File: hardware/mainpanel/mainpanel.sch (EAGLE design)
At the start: 0 parts

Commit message: Add Nucleo board
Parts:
- added B1: (no value), Frcy:NUCLEO-32

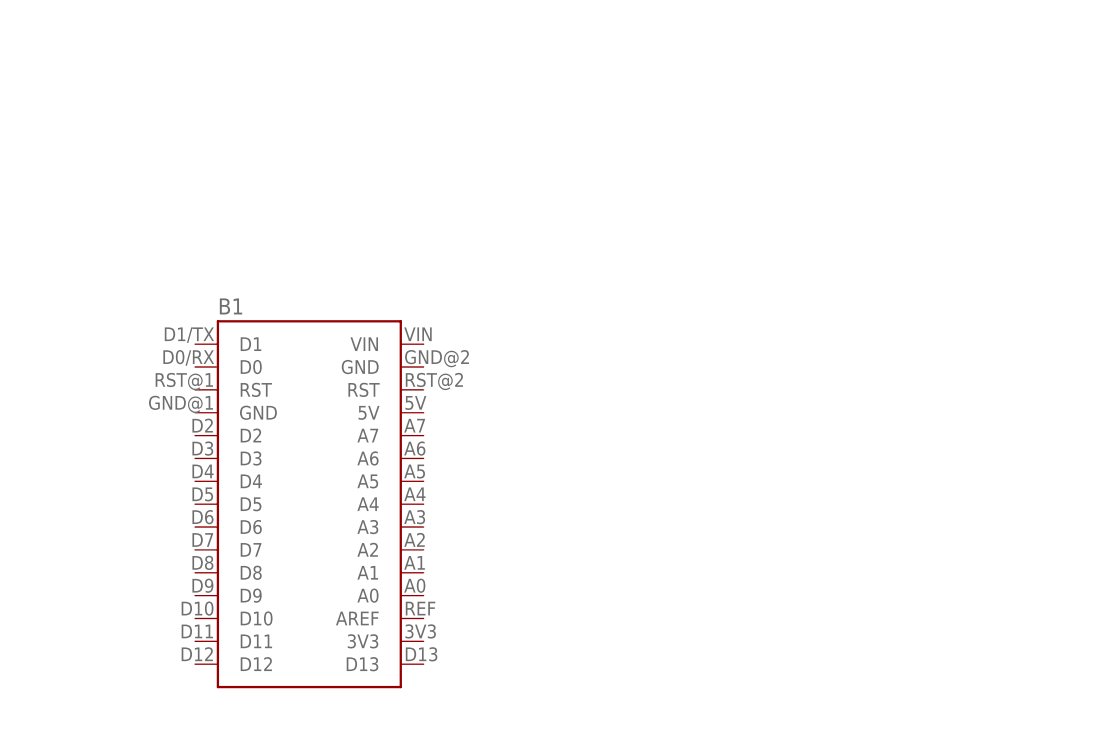
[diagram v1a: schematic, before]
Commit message: Add BNO055 and connections
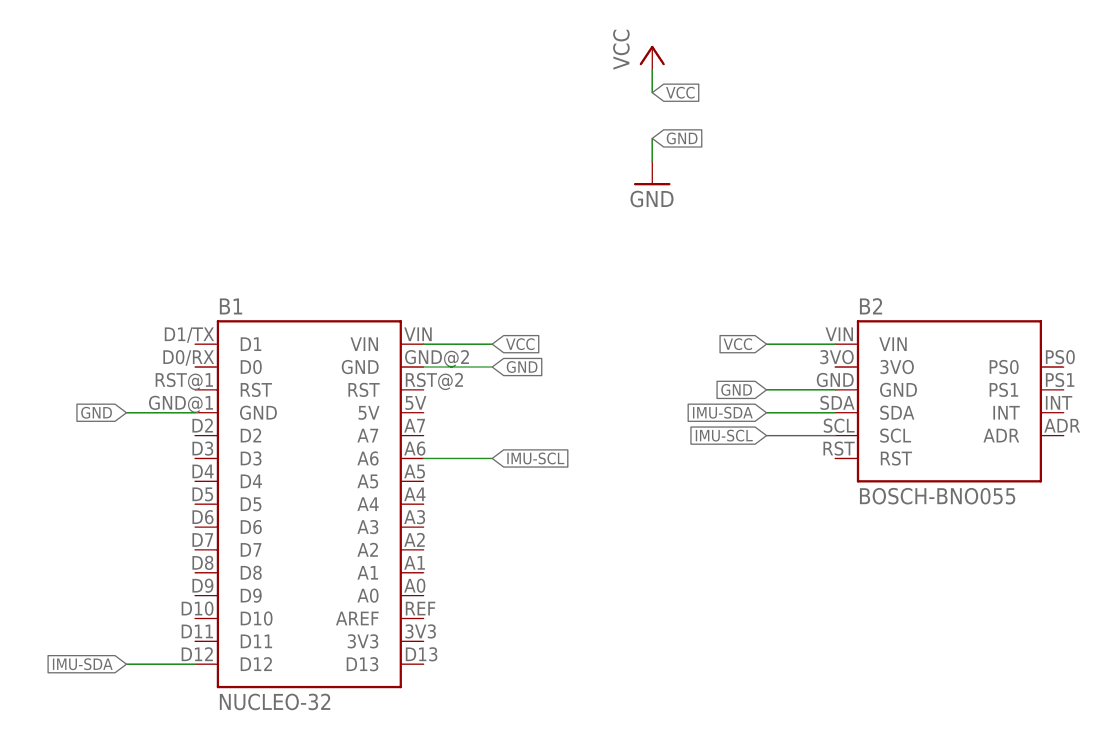
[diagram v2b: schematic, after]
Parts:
- added B2: BOSCH-BNO055, Frcy:BOSCH-BNO055
- B1: value (none) -> NUCLEO-32
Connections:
- new net GND: B1.GND@1, B1.GND@2, B2.GND
- new net IMU-SCL: B1.A6, B2.SCL
- new net IMU-SDA: B1.D12, B2.SDA
- new net VCC: B1.VIN, B2.VIN
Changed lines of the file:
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@@
 <part name="FRAME1" library="frames" library_urn="urn:adsk.eagle:library:229" deviceset="DINA4_L" device=""/>
 <part name="B1" library="Frcy" deviceset="NUCLEO-32" device=""/>
+<part name="B2" library="Frcy" deviceset="BOSCH-BNO055" device=""/>
+<part name="P+1" library="supply1" library_urn="urn:adsk.eagle:library:371" deviceset="VCC" device=""/>
+<part name="GND1" library="supply1" library_urn="urn:adsk.eagle:library:371" deviceset="GND" device=""/>
 </parts>
 <sheets>
@@
 <instance part="FRAME1" gate="G$2" x="162.56" y="0"/>
 <instance part="B1" gate="G$1" x="119.38" y="106.68"/>
+<instance part="B2" gate="G$1" x="190.5" y="119.38"/>
+<instance part="P+1" gate="VCC" x="157.48" y="157.48"/>
+<instance part="GND1" gate="1" x="157.48" y="142.24"/>
 </instances>
 <busses>
 </busses>
 <nets>
+<net name="VCC" class="0">
+<segment>
+<pinref part="P+1" gate="VCC" pin="VCC"/>
+<wire x1="157.48" y1="154.94" x2="157.48" y2="152.4" width="0.1524" layer="91"/>
+<label x="157.48" y="152.4" size="1.27" layer="95" xref="yes"/>
+</segment>
+<segment>
+<pinref part="B1" gate="G$1" pin="VIN"/>
+<wire x1="132.08" y1="124.46" x2="139.7" y2="124.46" width="0.1524" layer="91"/>
+<label x="139.7" y="124.46" size="1.27" layer="95" xref="yes"/>
+</segment>
+<segment>
+<pinref part="B2" gate="G$1" pin="VIN"/>
+<wire x1="177.8" y1="124.46" x2="170.18" y2="124.46" width="0.1524" layer="91"/>
+<label x="170.18" y="124.46" size="1.27" layer="95" rot="R180" xref="yes"/>
+</segment>
+</net>
+<net name="GND" class="0">
+<segment>
+<pinref part="GND1" gate="1" pin="GND"/>
+<wire x1="157.48" y1="144.78" x2="157.48" y2="147.32" width="0.1524" layer="91"/>
+<label x="157.48" y="147.32" size="1.27" layer="95" xref="yes"/>
+</segment>
+<segment>
+<pinref part="B1" gate="G$1" pin="GND@2"/>
+<wire x1="132.08" y1="121.92" x2="139.7" y2="121.92" width="0.1524" layer="91"/>
+<label x="139.7" y="121.92" size="1.27" layer="95" xref="yes"/>
+</segment>
+<segment>
+<pinref part="B1" gate="G$1" pin="GND@1"/>
+<wire x1="106.68" y1="116.84" x2="99.06" y2="116.84" width="0.1524" layer="91"/>
+<label x="99.06" y="116.84" size="1.27" layer="95" rot="R180" xref="yes"/>
+</segment>
+<segment>
+<pinref part="B2" gate="G$1" pin="GND"/>
+<wire x1="177.8" y1="119.38" x2="170.18" y2="119.38" width="0.1524" layer="91"/>
+<label x="170.18" y="119.38" size="1.27" layer="95" rot="R180" xref="yes"/>
+</segment>
+</net>
+<net name="IMU-SDA" class="0">
+<segment>
+<pinref part="B2" gate="G$1" pin="SDA"/>
+<wire x1="177.8" y1="116.84" x2="170.18" y2="116.84" width="0.1524" layer="91"/>
+<label x="170.18" y="116.84" size="1.27" layer="95" rot="R180" xref="yes"/>
+</segment>
+<segment>
+<pinref part="B1" gate="G$1" pin="D12"/>
+<wire x1="106.68" y1="88.9" x2="99.06" y2="88.9" width="0.1524" layer="91"/>
+<label x="99.06" y="88.9" size="1.27" layer="95" rot="R180" xref="yes"/>
+</segment>
+</net>
+<net name="IMU-SCL" class="0">
+<segment>
+<pinref part="B2" gate="G$1" pin="SCL"/>
+<wire x1="177.8" y1="114.3" x2="170.18" y2="114.3" width="0.1524" layer="91"/>
+<label x="170.18" y="114.3" size="1.27" layer="95" rot="R180" xref="yes"/>
+</segment>
+<segment>
+<pinref part="B1" gate="G$1" pin="A6"/>
+<wire x1="132.08" y1="111.76" x2="139.7" y2="111.76" width="0.1524" layer="91"/>
+<label x="139.7" y="111.76" size="1.27" layer="95" xref="yes"/>
+</segment>
+</net>
 </nets>
 </sheet>

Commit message: Add components to sch
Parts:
- added B3: (no value), Frcy:UPUTRONICS-UBLOX-PICO
- added B4: (no value), Frcy:SPARKFUN-OPENLOG
- B1: value NUCLEO-32 -> (none)
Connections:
- new net CDH-RX: B1.D0
- new net CDH-TX: B1.D1
- new net GPS-SCL: B1.D5, B3.SCL
- new net GPS-SDA: B1.D4, B3.SDA
- new net LOG-UART: B1.A7, B4.RXI
- new net SPI-CS-ADC: B1.D6
- new net SPI-CS-ENV: B1.D3
- new net SPI-MISO: B1.A5
- new net SPI-MOSI: B1.D2
- new net SPI-SCK: B1.A1
- new net TEMP-OW: B1.D9
- net GND: now also B3.GND, B4.GND
- net VCC: now also B3.VCC, B4.VCC
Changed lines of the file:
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@@
 <part name="P+1" library="supply1" library_urn="urn:adsk.eagle:library:371" deviceset="VCC" device=""/>
 <part name="GND1" library="supply1" library_urn="urn:adsk.eagle:library:371" deviceset="GND" device=""/>
+<part name="B3" library="Frcy" deviceset="UPUTRONICS-UBLOX-PICO" device=""/>
+<part name="B4" library="Frcy" deviceset="SPARKFUN-OPENLOG" device=""/>
 </parts>
 <sheets>
@@
 <instance part="P+1" gate="VCC" x="157.48" y="157.48"/>
 <instance part="GND1" gate="1" x="157.48" y="142.24"/>
+<instance part="B3" gate="G$1" x="182.88" y="91.44"/>
+<instance part="B4" gate="G$1" x="185.42" y="66.04"/>
 </instances>
 <busses>
@@
 <wire x1="177.8" y1="124.46" x2="170.18" y2="124.46" width="0.1524" layer="91"/>
 <label x="170.18" y="124.46" size="1.27" layer="95" rot="R180" xref="yes"/>
+</segment>
+<segment>
+<pinref part="B3" gate="G$1" pin="VCC"/>
+<wire x1="177.8" y1="86.36" x2="170.18" y2="86.36" width="0.1524" layer="91"/>
+<label x="170.18" y="86.36" size="1.27" layer="95" rot="R180" xref="yes"/>
+</segment>
+<segment>
+<pinref part="B4" gate="G$1" pin="VCC"/>
+<wire x1="177.8" y1="66.04" x2="170.18" y2="66.04" width="0.1524" layer="91"/>
+<label x="170.18" y="66.04" size="1.27" layer="95" rot="R180" xref="yes"/>
 </segment>
 </net>
@@
 <wire x1="177.8" y1="119.38" x2="170.18" y2="119.38" width="0.1524" layer="91"/>
 <label x="170.18" y="119.38" size="1.27" layer="95" rot="R180" xref="yes"/>
+</segment>
+<segment>
+<pinref part="B3" gate="G$1" pin="GND"/>
+<wire x1="177.8" y1="88.9" x2="170.18" y2="88.9" width="0.1524" layer="91"/>
+<label x="170.18" y="88.9" size="1.27" layer="95" rot="R180" xref="yes"/>
+</segment>
+<segment>
+<pinref part="B4" gate="G$1" pin="GND"/>
+<wire x1="177.8" y1="63.5" x2="170.18" y2="63.5" width="0.1524" layer="91"/>
+<label x="170.18" y="63.5" size="1.27" layer="95" rot="R180" xref="yes"/>
 </segment>
 </net>
@@
 </segment>
 </net>
+<net name="GPS-SDA" class="0">
+<segment>
+<pinref part="B3" gate="G$1" pin="SDA"/>
+<wire x1="177.8" y1="99.06" x2="170.18" y2="99.06" width="0.1524" layer="91"/>
+<label x="170.18" y="99.06" size="1.27" layer="95" rot="R180" xref="yes"/>
+</segment>
+<segment>
+<pinref part="B1" gate="G$1" pin="D4"/>
+<wire x1="106.68" y1="109.22" x2="99.06" y2="109.22" width="0.1524" layer="91"/>
+<label x="99.06" y="109.22" size="1.27" layer="95" rot="R180" xref="yes"/>
+</segment>
+</net>
+<net name="GPS-SCL" class="0">
+<segment>
+<pinref part="B3" gate="G$1" pin="SCL"/>
+<wire x1="177.8" y1="96.52" x2="170.18" y2="96.52" width="0.1524" layer="91"/>
+<label x="170.18" y="96.52" size="1.27" layer="95" rot="R180" xref="yes"/>
+</segment>
+<segment>
+<pinref part="B1" gate="G$1" pin="D5"/>
+<wire x1="106.68" y1="106.68" x2="99.06" y2="106.68" width="0.1524" layer="91"/>
+<label x="99.06" y="106.68" size="1.27" layer="95" rot="R180" xref="yes"/>
+</segment>
+</net>
+<net name="LOG-UART" class="0">
+<segment>
+<pinref part="B4" gate="G$1" pin="RXI"/>
+<wire x1="177.8" y1="71.12" x2="170.18" y2="71.12" width="0.1524" layer="91"/>
+<label x="170.18" y="71.12" size="1.27" layer="95" rot="R180" xref="yes"/>
+</segment>
+<segment>
+<pinref part="B1" gate="G$1" pin="A7"/>
+<wire x1="132.08" y1="114.3" x2="139.7" y2="114.3" width="0.1524" layer="91"/>
+<label x="139.7" y="114.3" size="1.27" layer="95" xref="yes"/>
+</segment>
+</net>
+<net name="CDH-TX" class="0">
+<segment>
+<pinref part="B1" gate="G$1" pin="D1"/>
+<wire x1="106.68" y1="124.46" x2="99.06" y2="124.46" width="0.1524" layer="91"/>
+<label x="99.06" y="124.46" size="1.27" layer="95" rot="R180" xref="yes"/>
+</segment>
+</net>
+<net name="CDH-RX" class="0">
+<segment>
+<pinref part="B1" gate="G$1" pin="D0"/>
+<wire x1="106.68" y1="121.92" x2="99.06" y2="121.92" width="0.1524" layer="91"/>
+<label x="99.06" y="121.92" size="1.27" layer="95" rot="R180" xref="yes"/>
+</segment>
+</net>
+<net name="SPI-MOSI" class="0">
+<segment>
+<pinref part="B1" gate="G$1" pin="D2"/>
+<wire x1="106.68" y1="114.3" x2="99.06" y2="114.3" width="0.1524" layer="91"/>
+<label x="99.06" y="114.3" size="1.27" layer="95" rot="R180" xref="yes"/>
+</segment>
+</net>
+<net name="SPI-CS-ADC" class="0">
+<segment>
+<pinref part="B1" gate="G$1" pin="D6"/>
+<wire x1="106.68" y1="104.14" x2="99.06" y2="104.14" width="0.1524" layer="91"/>
+<label x="99.06" y="104.14" size="1.27" layer="95" rot="R180" xref="yes"/>
+</segment>
+</net>
+<net name="TEMP-OW" class="0">
+<segment>
+<pinref part="B1" gate="G$1" pin="D9"/>
+<wire x1="106.68" y1="96.52" x2="99.06" y2="96.52" width="0.1524" layer="91"/>
+<label x="99.06" y="96.52" size="1.27" layer="95" rot="R180" xref="yes"/>
+</segment>
+</net>
+<net name="SPI-SCK" class="0">
+<segment>
+<pinref part="B1" gate="G$1" pin="A1"/>
+<wire x1="132.08" y1="99.06" x2="139.7" y2="99.06" width="0.1524" layer="91"/>
+<label x="139.7" y="99.06" size="1.27" layer="95" xref="yes"/>
+</segment>
+</net>
+<net name="SPI-MISO" class="0">
+<segment>
+<pinref part="B1" gate="G$1" pin="A5"/>
+<wire x1="132.08" y1="109.22" x2="139.7" y2="109.22" width="0.1524" layer="91"/>
+<label x="139.7" y="109.22" size="1.27" layer="95" xref="yes"/>
+</segment>
+</net>
+<net name="SPI-CS-ENV" class="0">
+<segment>
+<pinref part="B1" gate="G$1" pin="D3"/>
+<wire x1="106.68" y1="111.76" x2="99.06" y2="111.76" width="0.1524" layer="91"/>
+<label x="99.06" y="111.76" size="1.27" layer="95" rot="R180" xref="yes"/>
+</segment>
+</net>

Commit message: Add connectors
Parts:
- added J1, J2, J3: 90136-104, con-molex-c-grid:90136-104
- added J4: 90136-108, con-molex-c-grid:90136-108
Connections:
- new net N$1: J3.1
- new net N$10: J4.6
- new net N$11: J4.7
- new net N$12: J4.8
- new net N$2: J3.2
- new net N$3: J3.3
- new net N$4: J3.4
- new net N$5: J4.1
- new net N$6: J4.2
- new net N$7: J4.3
- new net N$8: J4.4
- new net N$9: J4.5
- net CDH-RX: now also J1.3
- net CDH-TX: now also J1.2
- net GND: now also J1.1, J2.1, J2.3
- net TEMP-OW: now also J2.2
- net VCC: now also J1.4, J2.4
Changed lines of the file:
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@@
 </variantdefs>
 <classes>
-<class number="0" name="default" width="0" drill="0">
+<class number="0" name="default" width="0.8128" drill="0.8">
+<clearance class="0" value="0.4064"/>
 </class>
 </classes>
@@
 <part name="B3" library="Frcy" deviceset="UPUTRONICS-UBLOX-PICO" device=""/>
 <part name="B4" library="Frcy" deviceset="SPARKFUN-OPENLOG" device=""/>
+<part name="J1" library="con-molex-c-grid" deviceset="90136-1?04" device=""/>
+<part name="J2" library="con-molex-c-grid" deviceset="90136-1?04" device=""/>
+<part name="J3" library="con-molex-c-grid" deviceset="90136-1?04" device=""/>
+<part name="J4" library="con-molex-c-grid" deviceset="90136-1?08" device=""/>
 </parts>
 <sheets>
@@
 <instance part="B3" gate="G$1" x="182.88" y="91.44"/>
 <instance part="B4" gate="G$1" x="185.42" y="66.04"/>
+<instance part="J1" gate="G$1" x="50.8" y="124.46" rot="MR0"/>
+<instance part="J2" gate="G$1" x="50.8" y="104.14" rot="MR0"/>
+<instance part="J3" gate="G$1" x="50.8" y="83.82" rot="MR0"/>
+<instance part="J4" gate="G$1" x="50.8" y="58.42" rot="MR0"/>
 </instances>
 <busses>
@@
 <label x="170.18" y="66.04" size="1.27" layer="95" rot="R180" xref="yes"/>
 </segment>
+<segment>
+<pinref part="J1" gate="G$1" pin="4"/>
+<wire x1="55.88" y1="119.38" x2="63.5" y2="119.38" width="0.1524" layer="91"/>
+<label x="63.5" y="119.38" size="1.27" layer="95" xref="yes"/>
+</segment>
+<segment>
+<pinref part="J2" gate="G$1" pin="4"/>
+<wire x1="55.88" y1="99.06" x2="63.5" y2="99.06" width="0.1524" layer="91"/>
+<label x="63.5" y="99.06" size="1.27" layer="95" xref="yes"/>
+</segment>
 </net>
 <net name="GND" class="0">
@@
 <label x="170.18" y="63.5" size="1.27" layer="95" rot="R180" xref="yes"/>
 </segment>
+<segment>
+<pinref part="J1" gate="G$1" pin="1"/>
+<wire x1="55.88" y1="127" x2="63.5" y2="127" width="0.1524" layer="91"/>
+<label x="63.5" y="127" size="1.27" layer="95" xref="yes"/>
+</segment>
+<segment>
+<pinref part="J2" gate="G$1" pin="1"/>
+<wire x1="55.88" y1="106.68" x2="63.5" y2="106.68" width="0.1524" layer="91"/>
+<label x="63.5" y="106.68" size="1.27" layer="95" xref="yes"/>
+</segment>
+<segment>
+<pinref part="J2" gate="G$1" pin="3"/>
+<wire x1="55.88" y1="101.6" x2="63.5" y2="101.6" width="0.1524" layer="91"/>
+<label x="63.5" y="101.6" size="1.27" layer="95" xref="yes"/>
+</segment>
 </net>
 <net name="IMU-SDA" class="0">
@@
 <label x="99.06" y="124.46" size="1.27" layer="95" rot="R180" xref="yes"/>
 </segment>
+<segment>
+<pinref part="J1" gate="G$1" pin="2"/>
+<wire x1="55.88" y1="124.46" x2="63.5" y2="124.46" width="0.1524" layer="91"/>
+<label x="63.5" y="124.46" size="1.27" layer="95" xref="yes"/>
+</segment>
 </net>
 <net name="CDH-RX" class="0">
@@
 <label x="99.06" y="121.92" size="1.27" layer="95" rot="R180" xref="yes"/>
 </segment>
+<segment>
+<pinref part="J1" gate="G$1" pin="3"/>
+<wire x1="55.88" y1="121.92" x2="63.5" y2="121.92" width="0.1524" layer="91"/>
+<label x="63.5" y="121.92" size="1.27" layer="95" xref="yes"/>
+</segment>
 </net>
 <net name="SPI-MOSI" class="0">
@@
 <label x="99.06" y="96.52" size="1.27" layer="95" rot="R180" xref="yes"/>
 </segment>
+<segment>
+<pinref part="J2" gate="G$1" pin="2"/>
+<wire x1="55.88" y1="104.14" x2="63.5" y2="104.14" width="0.1524" layer="91"/>
+<label x="63.5" y="104.14" size="1.27" layer="95" xref="yes"/>
+</segment>
 </net>
 <net name="SPI-SCK" class="0">
@@
 </segment>
 </net>
+<net name="N$1" class="0">
+<segment>
+<pinref part="J3" gate="G$1" pin="1"/>
+<wire x1="55.88" y1="86.36" x2="63.5" y2="86.36" width="0.1524" layer="91"/>
+<label x="63.5" y="86.36" size="1.27" layer="95" xref="yes"/>
+</segment>
+</net>
+<net name="N$2" class="0">
+<segment>
+<pinref part="J3" gate="G$1" pin="2"/>
+<wire x1="55.88" y1="83.82" x2="63.5" y2="83.82" width="0.1524" layer="91"/>
+<label x="63.5" y="83.82" size="1.27" layer="95" xref="yes"/>
+</segment>
+</net>
+<net name="N$3" class="0">
+<segment>
+<pinref part="J3" gate="G$1" pin="3"/>
+<wire x1="55.88" y1="81.28" x2="63.5" y2="81.28" width="0.1524" layer="91"/>
+<label x="63.5" y="81.28" size="1.27" layer="95" xref="yes"/>
+</segment>
+</net>
+<net name="N$4" class="0">
+<segment>
+<pinref part="J3" gate="G$1" pin="4"/>
+<wire x1="55.88" y1="78.74" x2="63.5" y2="78.74" width="0.1524" layer="91"/>
+<label x="63.5" y="78.74" size="1.27" layer="95" xref="yes"/>
+</segment>
+</net>
+<net name="N$5" class="0">
+<segment>
+<pinref part="J4" gate="G$1" pin="1"/>
+<wire x1="55.88" y1="66.04" x2="63.5" y2="66.04" width="0.1524" layer="91"/>
+</segment>
+</net>
+<net name="N$6" class="0">
+<segment>
+<pinref part="J4" gate="G$1" pin="2"/>
+<wire x1="55.88" y1="63.5" x2="63.5" y2="63.5" width="0.1524" layer="91"/>
+</segment>
+</net>
+<net name="N$7" class="0">
+<segment>
+<pinref part="J4" gate="G$1" pin="3"/>
+<wire x1="55.88" y1="60.96" x2="63.5" y2="60.96" width="0.1524" layer="91"/>
+</segment>
+</net>
+<net name="N$8" class="0">
+<segment>
+<pinref part="J4" gate="G$1" pin="4"/>
+<wire x1="55.88" y1="58.42" x2="63.5" y2="58.42" width="0.1524" layer="91"/>
+</segment>
+</net>
+<net name="N$9" class="0">
+<segment>
+<pinref part="J4" gate="G$1" pin="5"/>
+<wire x1="55.88" y1="55.88" x2="63.5" y2="55.88" width="0.1524" layer="91"/>
+</segment>
+</net>
+<net name="N$10" class="0">
+<segment>
+<pinref part="J4" gate="G$1" pin="6"/>
+<wire x1="55.88" y1="53.34" x2="63.5" y2="53.34" width="0.1524" layer="91"/>
+</segment>
+</net>
+<net name="N$11" class="0">
+<segment>
+<pinref part="J4" gate="G$1" pin="7"/>
+<wire x1="55.88" y1="50.8" x2="63.5" y2="50.8" width="0.1524" layer="91"/>
+</segment>
+</net>
+<net name="N$12" class="0">
+<segment>
+<pinref part="J4" gate="G$1" pin="8"/>
+<wire x1="55.88" y1="48.26" x2="63.5" y2="48.26" width="0.1524" layer="91"/>
+</segment>
+</net>

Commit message: Add more connectors
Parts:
- added J5: 90136-104, con-molex-c-grid:90136-104
- J1: value 90136-104 -> 90136-106; device con-molex-c-grid:90136-104 -> con-molex-c-grid:90136-106
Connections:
- removed net N$1: J3.1
- removed net N$10: J4.6
- removed net N$11: J4.7
- removed net N$12: J4.8
- removed net N$2: J3.2
- removed net N$3: J3.3
- removed net N$4: J3.4
- removed net N$5: J4.1
- removed net N$6: J4.2
- removed net N$7: J4.3
- removed net N$8: J4.4
- removed net N$9: J4.5
- removed net SPI-CS-ADC: B1.D6
- new net DBG-RX: B1.A2, J3.3
- new net DBG-TX: B1.A0, J3.4
- new net GPS-RX: B3.RXD, J3.1
- new net GPS-TX: B3.TXD, J3.2
- new net N$13: B1.RST@2
- new net SPI-CS-ADCS: B1.D6, J4.2
- new net SPI-CS-SUN: B1.D10, J4.3
- new net SUN-RX: B1.A4, J5.2
- new net SUN-TX: B1.A3, J5.3
- net CDH-RX: now also J1.4; no longer J1.3
- net CDH-TX: now also J1.3; no longer J1.2
- net GND: now also J1.5, J1.6, J4.5, J5.1
- net SPI-CS-ENV: now also J4.1
- net SPI-MISO: now also J4.6
- net SPI-MOSI: now also J4.7
- net SPI-SCK: now also J4.4
- net VCC: now also B1.3V3, J1.2, J4.8, J5.4; no longer B1.VIN, J1.4

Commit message: Add values for parts
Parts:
- B1: value (none) -> NUCLEO-32
- B3: value (none) -> UPUTRONICS-UBLOX-PICO
- B4: value (none) -> SPARKFUN-OPENLOG
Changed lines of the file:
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@@
 <parts>
 <part name="FRAME1" library="frames" library_urn="urn:adsk.eagle:library:229" deviceset="DINA4_L" device=""/>
-<part name="B1" library="Frcy" deviceset="NUCLEO-32" device=""/>
+<part name="B1" library="Frcy" deviceset="NUCLEO-32" device="" value="NUCLEO-32"/>
 <part name="B2" library="Frcy" deviceset="BOSCH-BNO055" device=""/>
 <part name="P+1" library="supply1" library_urn="urn:adsk.eagle:library:371" deviceset="VCC" device=""/>
 <part name="GND1" library="supply1" library_urn="urn:adsk.eagle:library:371" deviceset="GND" device=""/>
-<part name="B3" library="Frcy" deviceset="UPUTRONICS-UBLOX-PICO" device=""/>
-<part name="B4" library="Frcy" deviceset="SPARKFUN-OPENLOG" device=""/>
+<part name="B3" library="Frcy" deviceset="UPUTRONICS-UBLOX-PICO" device="" value="UPUTRONICS-UBLOX-PICO"/>
+<part name="B4" library="Frcy" deviceset="SPARKFUN-OPENLOG" device="" value="SPARKFUN-OPENLOG"/>
 <part name="J2" library="con-molex-c-grid" deviceset="90136-1?04" device=""/>
 <part name="J3" library="con-molex-c-grid" deviceset="90136-1?04" device=""/>
